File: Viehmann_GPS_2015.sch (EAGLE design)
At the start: 16 parts

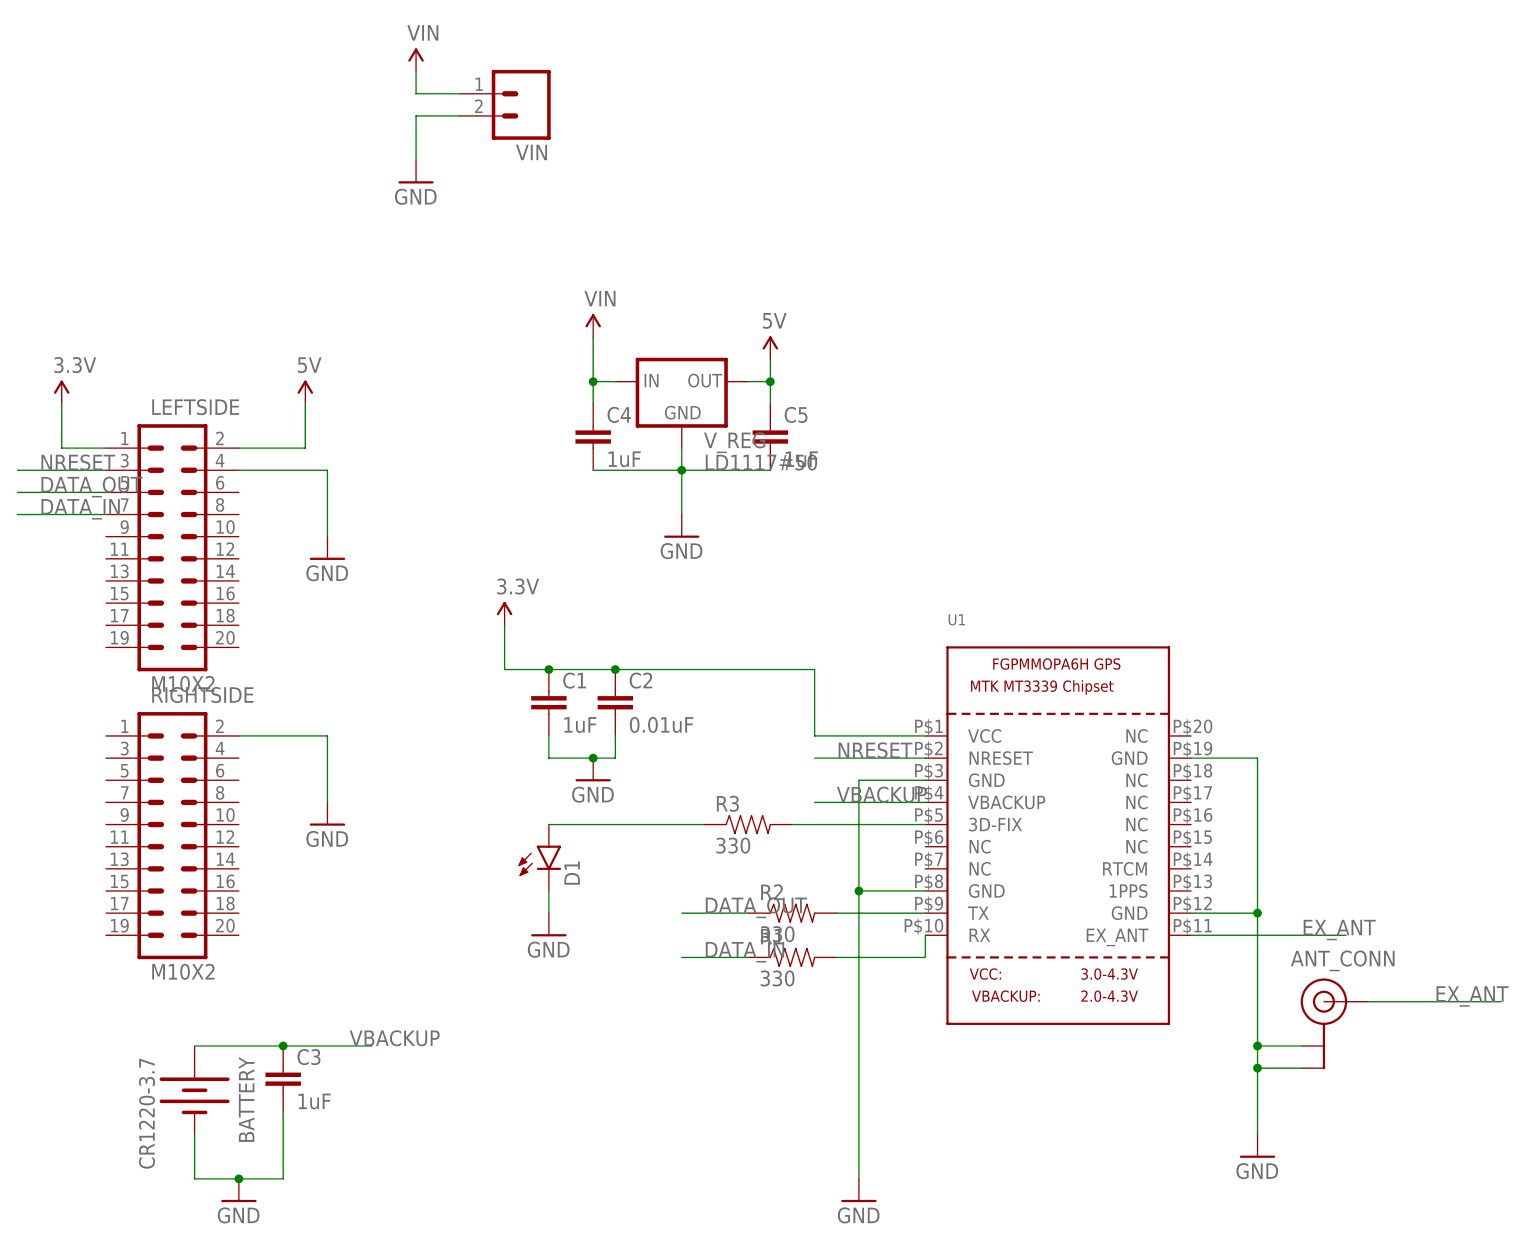
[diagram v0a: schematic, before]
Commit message: Removed unnessasary files and file structure
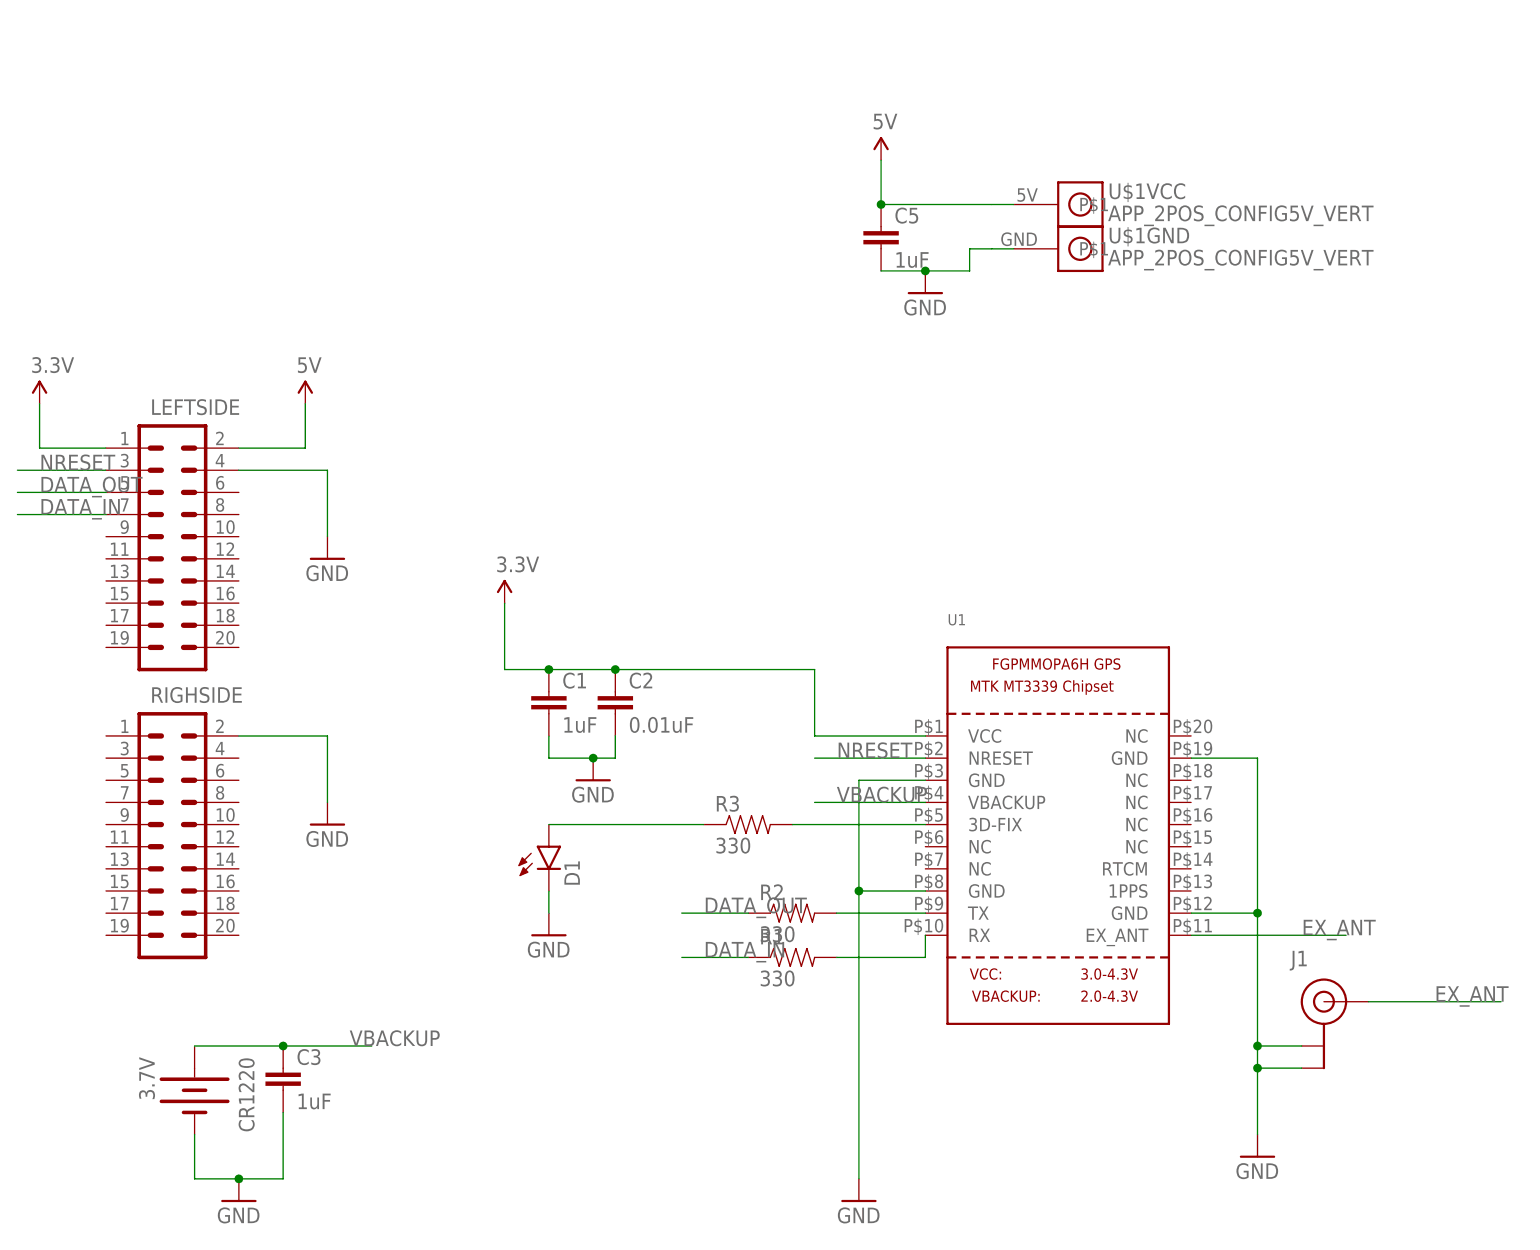
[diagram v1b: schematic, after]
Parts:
- removed C4: 1uF, SparkFun-Capacitors:CAP1206
- removed VIN: M02PTH, SparkFun-Connectors:M02PTH
- removed V_REG: LD1117#50, SparkFun-PowerIC:V_REG_MIC2920
- added U$1: APP_2POS_CONFIG5V_VERT, MRDT-Connectors:APP_2POS_CONFIG5V_VERT
- CR1220: value CR1220-3.7 -> 3.7V
- LEFTSIDE, RIGHSIDE: value M10X2 -> (none)
- renumbered ANT_CONN to J1, BATTERY to CR1220, RIGHTSIDE to RIGHSIDE
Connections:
- removed net VIN: C4.1, VIN.1, V_REG.IN
- net 5V: now also U$1VCC.P$1; no longer V_REG.OUT
- net GND: now also U$1GND.P$1; no longer C4.2, VIN.2, V_REG.GND
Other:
- moved on the sheet: C5
